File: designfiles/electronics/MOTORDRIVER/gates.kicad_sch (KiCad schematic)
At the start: 38 parts, among them IC14 LM5109BSDX_NOPB, IC15 LM5109BSDX_NOPB, IC16 LM5109BSDX_NOPB, IC17 LM5109BSDX_NOPB, IC18 INA2181A2IDGSR, Q22 30V 71A, Q23 30V 71A, Q24 30V 71A, Q25 30V 71A, Q26 30V 71A, Q27 30V 71A, Q28 30V 71A

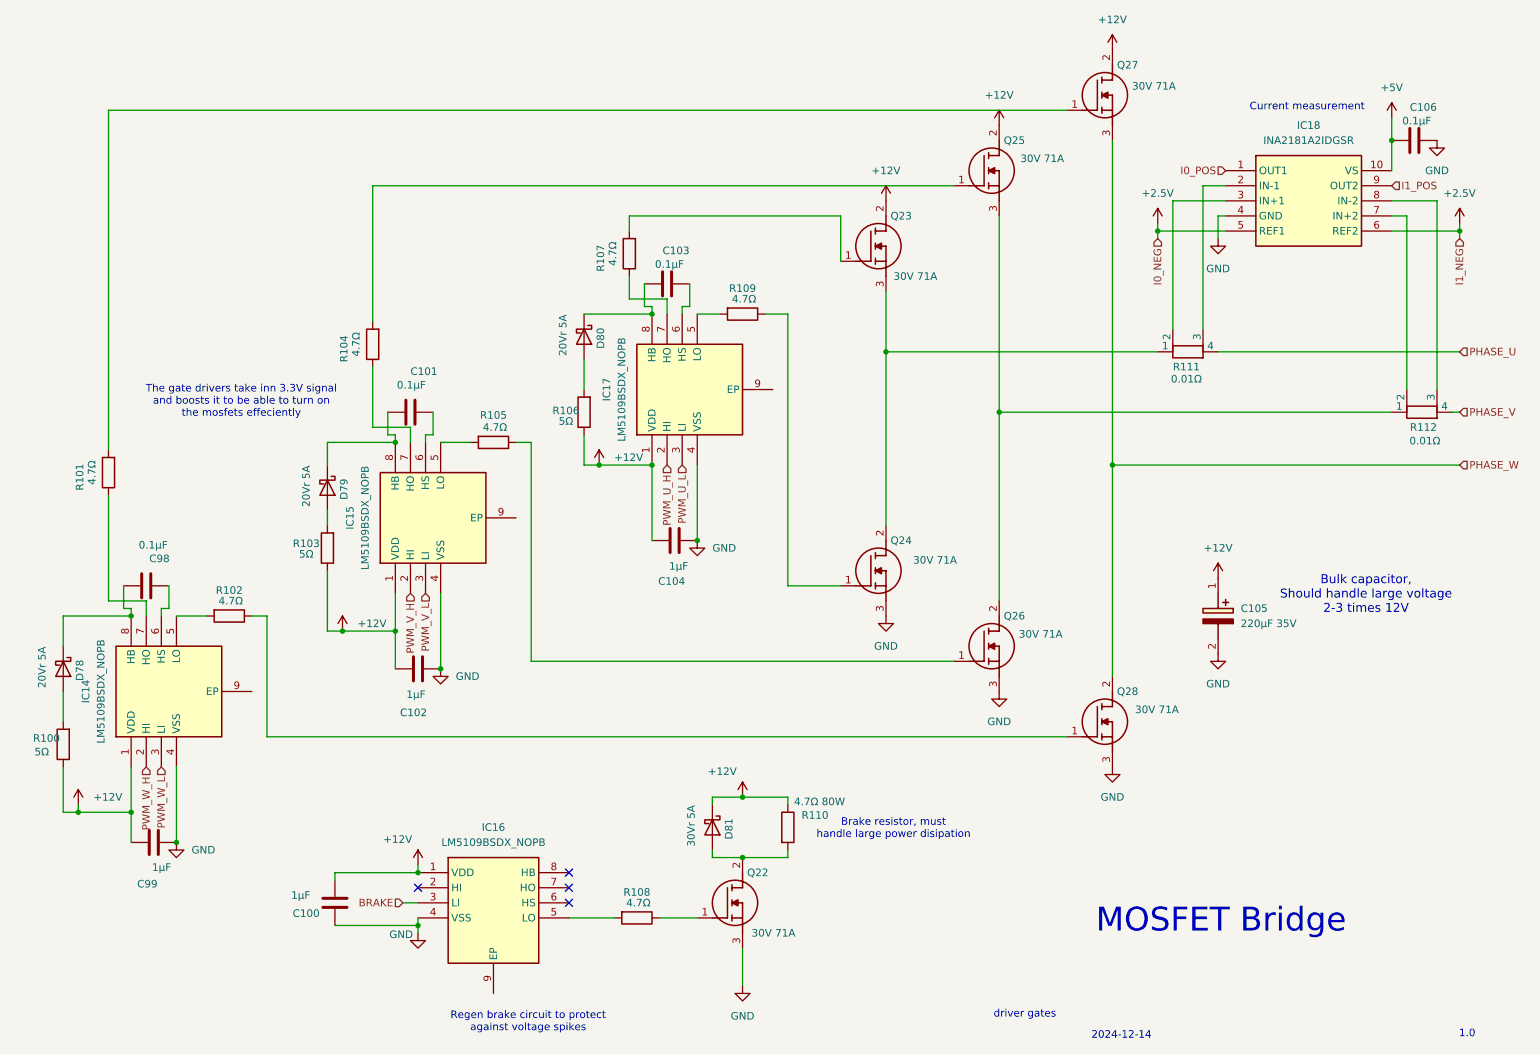
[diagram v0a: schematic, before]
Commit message: made clearer foldernames and cleaned up
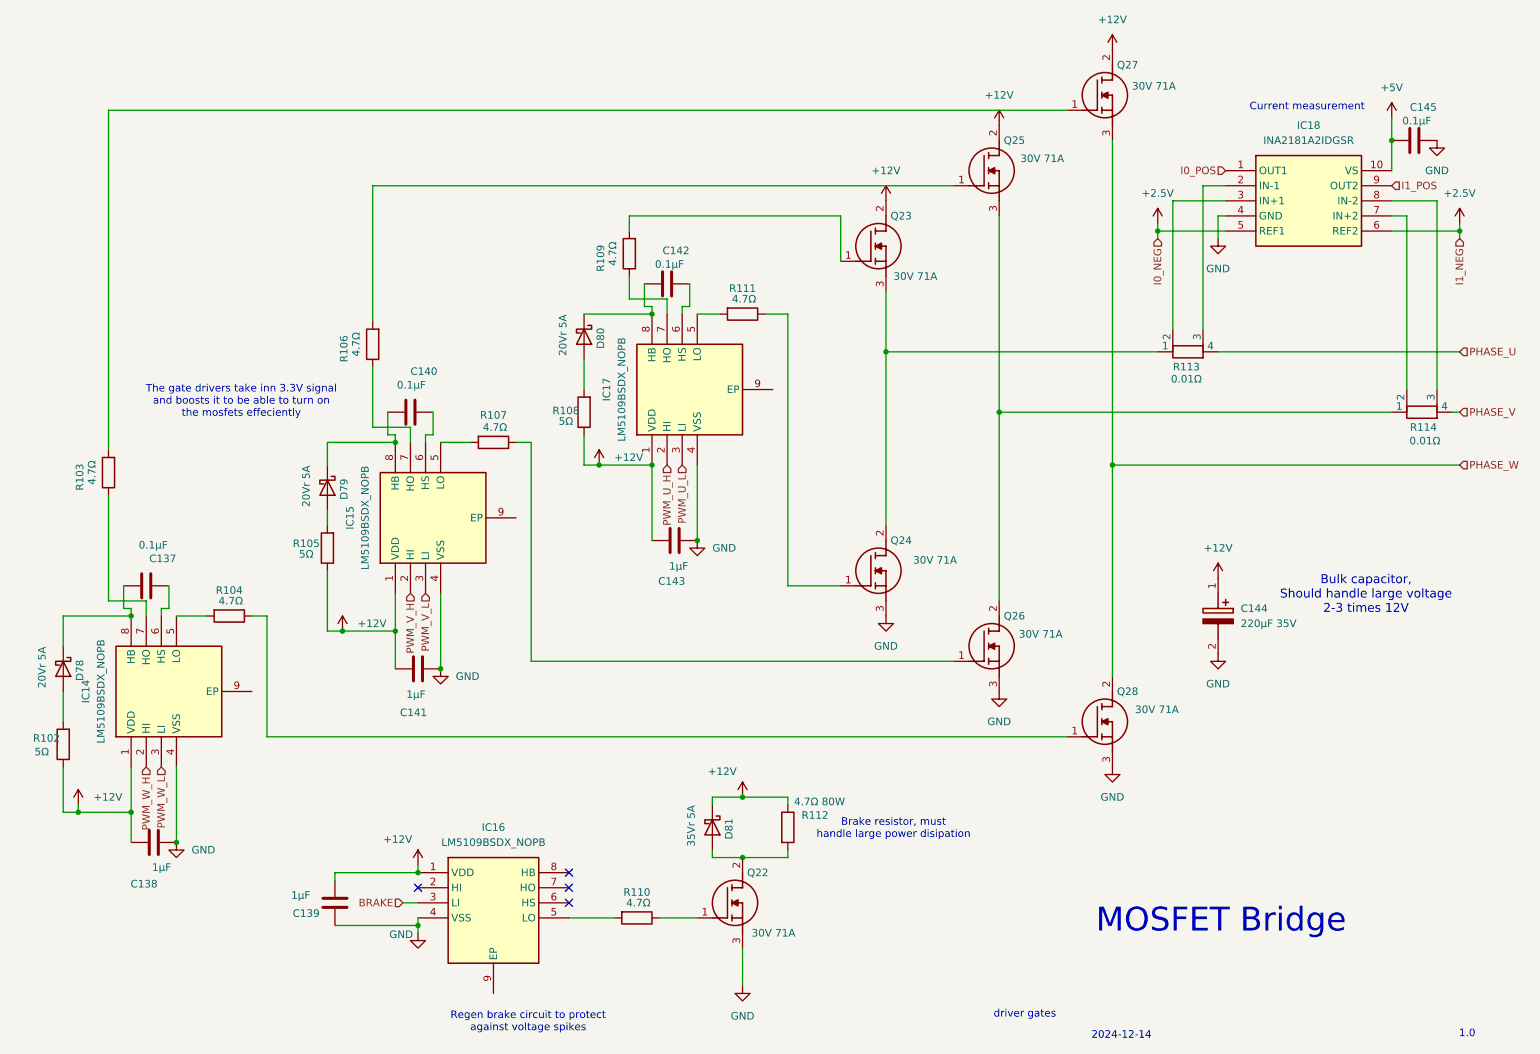
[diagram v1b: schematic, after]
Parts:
- D81: value 30Vr 5A -> 35Vr 5A
- renumbered C98 to C137, C99 to C138, C100 to C139, C101 to C140, C102 to C141, C103 to C142, C104 to C143, C105 to C144, C106 to C145, R100 to R102, R101 to R103, R102 to R104, R103 to R105, R104 to R106, R105 to R107, R106 to R108, R107 to R109, R108 to R110, R109 to R111, R110 to R112, R111 to R113, R112 to R114

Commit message: removed backup files and found components for special resistors and diodes
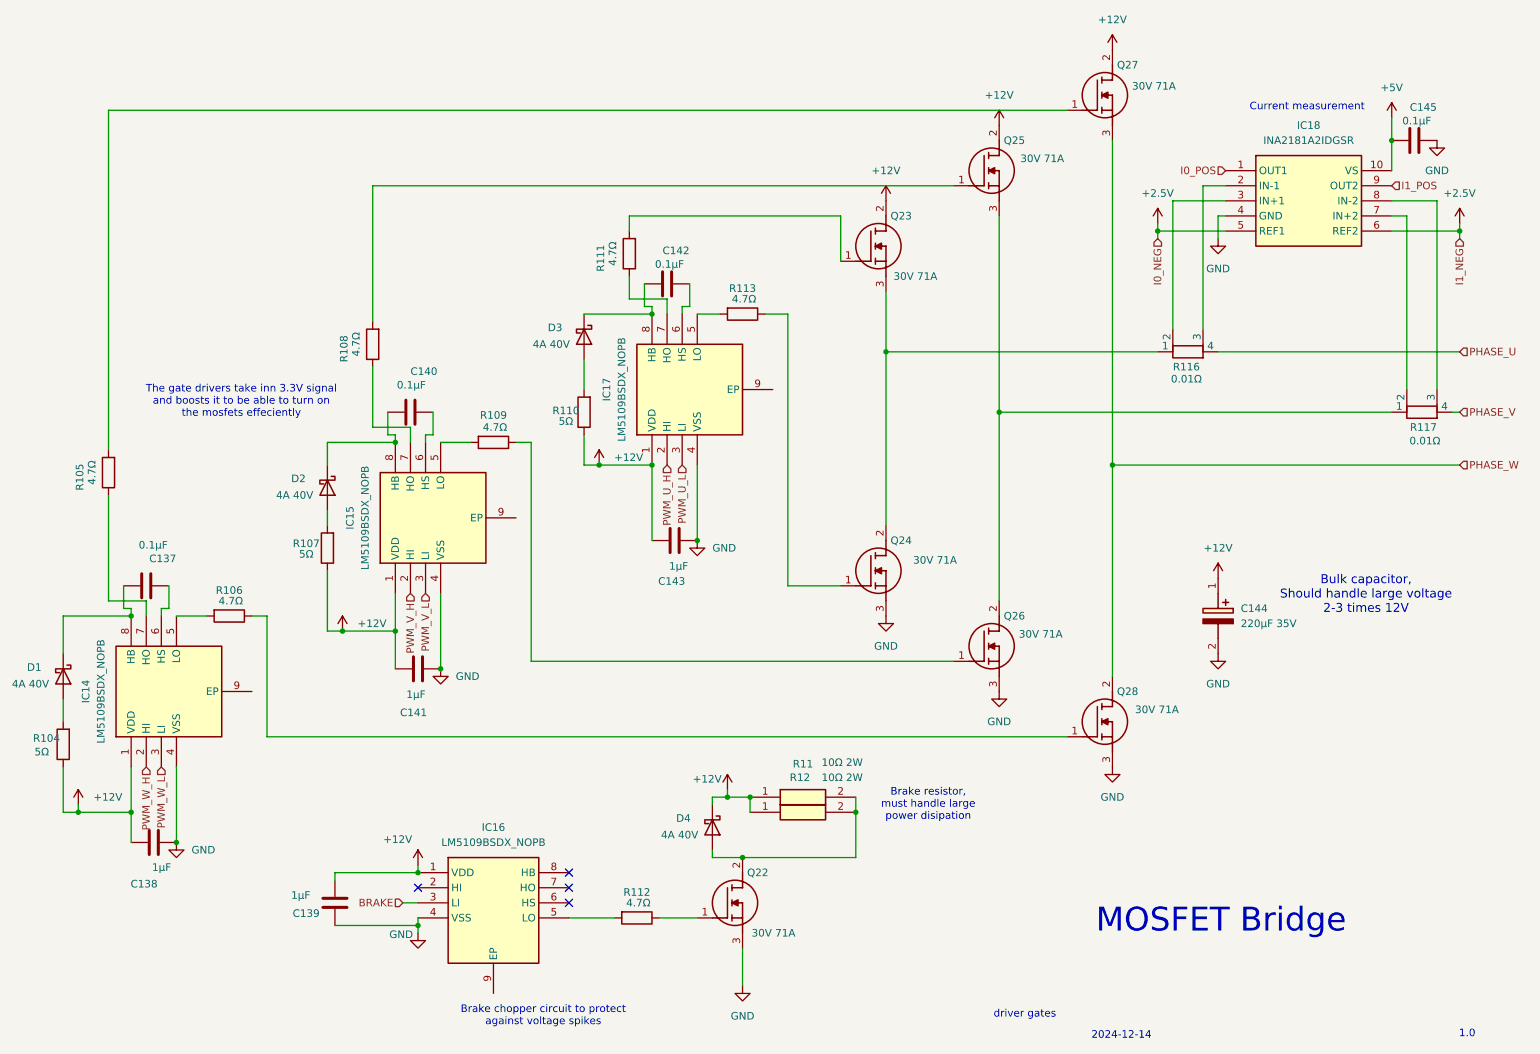
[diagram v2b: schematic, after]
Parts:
- removed D78, D79, D80: 20Vr 5A, Diode_SMD:D_0603_1608Metric, symbol Device:D_Schottky
- removed D81: 35Vr 5A, Diode_SMD:D_0603_1608Metric, symbol Device:D_Schottky
- removed R112: 4.7Ω 80W, Resistor_SMD:R_0603_1608Metric, symbol Device:R
- added D1, D2, D3, D4: 4A 40V, kuben-footprints:DIOM7959X262N, symbol Device:D_Schottky
- added R11, R12: 10Ω 2W, kuben-footprints:RESC3263X80N, symbol RCL122510R0FKEG:RCL122510R0FKEG
- renumbered R102 to R104, R103 to R105, R104 to R106, R105 to R107, R106 to R108, R107 to R109, R108 to R110, R109 to R111, R110 to R112, R111 to R113, R113 to R116, R114 to R117
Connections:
- net +12V: now also D4.1 (K), R11.1, R12.1
- net at R104.2: now also D1.2 (A)
- net at C140.2, IC15.8 (HB): now also D2.1 (K)
- net at C142.2, IC17.8 (HB): now also D3.1 (K)
- net at Q22.2 (D): now also D4.2 (A), R11.2, R12.2
- net at R110.2: now also D3.2 (A)
- net at C137.2, IC14.8 (HB): now also D1.1 (K)
- net at R107.2: now also D2.2 (A)
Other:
- note added: "Brake chopper circuit to protect against voltage spikes"
- note removed: "Regen brake circuit to protect against voltage spikes"

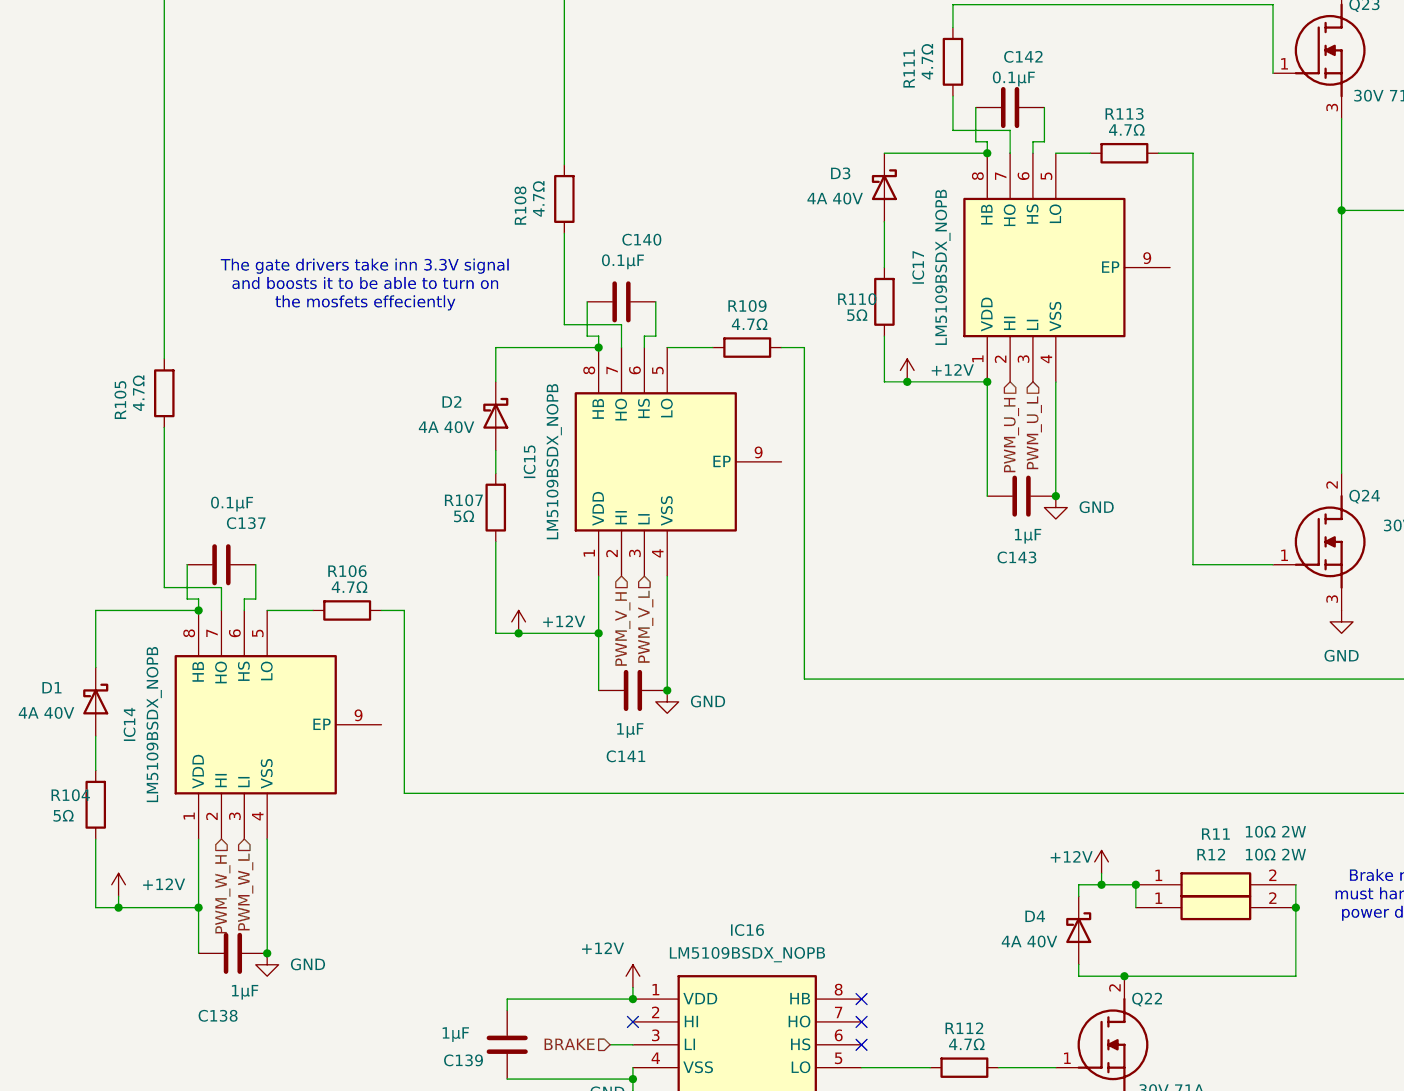
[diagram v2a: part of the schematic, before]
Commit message: added diodes
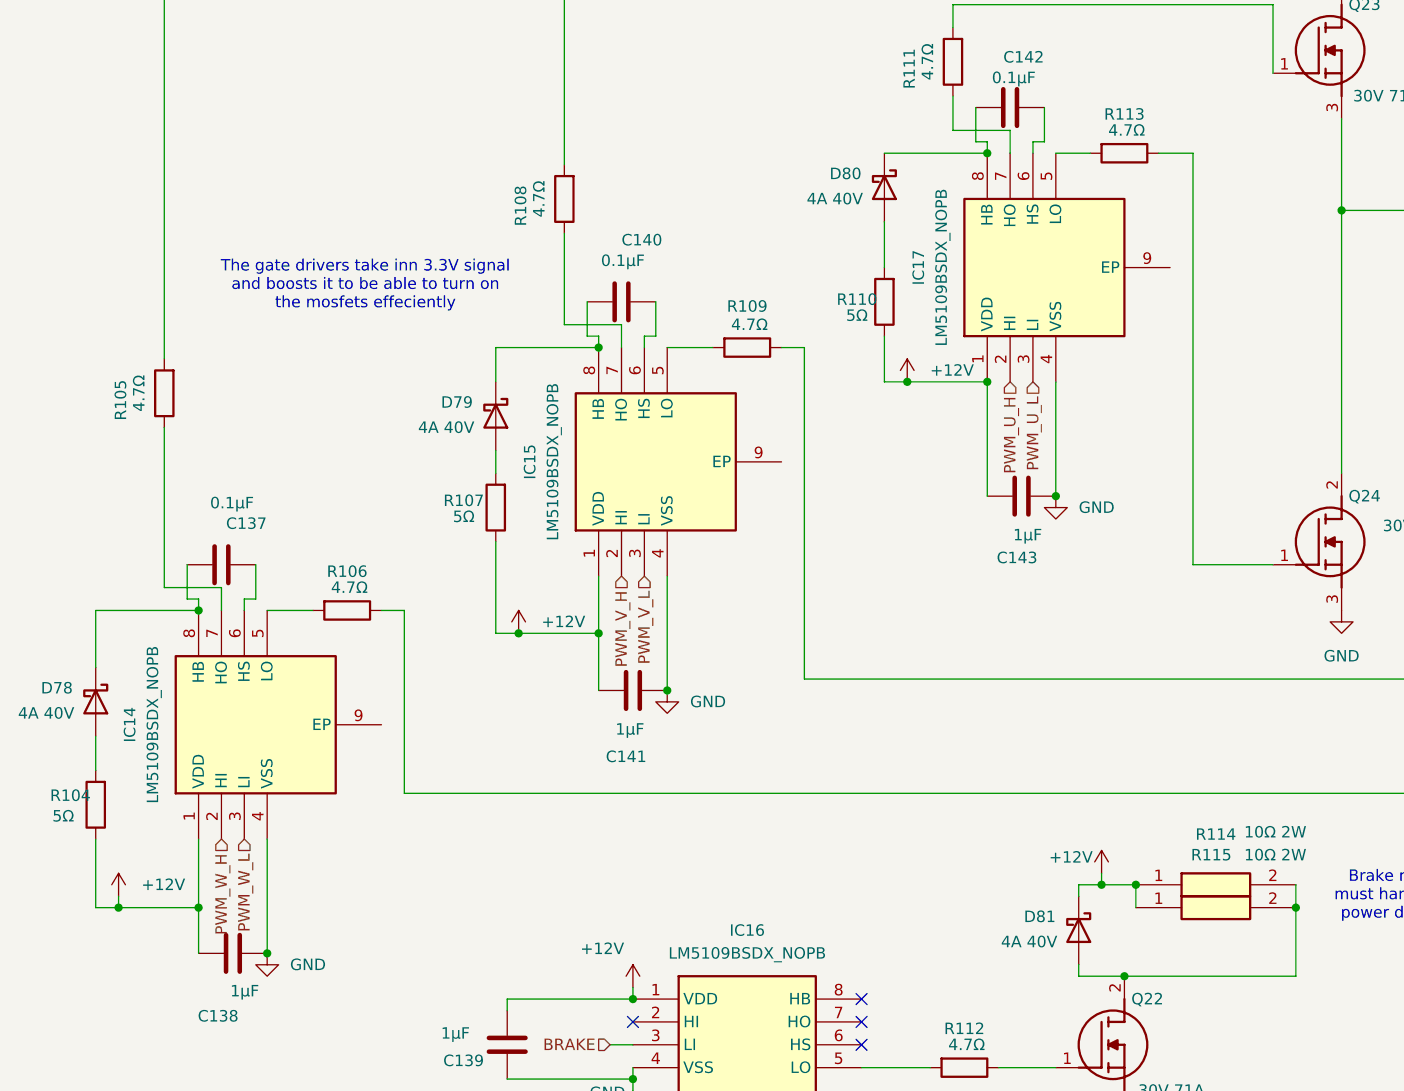
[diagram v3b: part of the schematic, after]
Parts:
- renumbered D1 to D78, D2 to D79, D3 to D80, D4 to D81, R11 to R114, R12 to R115
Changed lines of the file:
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@@
 		(on_board yes)
 		(dnp no)
-		(property "Reference" "D1"
+		(property "Reference" "D78"
 			(at 28.194 131.826 90)
 			(effects
@@
 		(on_board yes)
 		(dnp no)
-		(property "Reference" "D2"
+		(property "Reference" "D79"
 			(at 72.644 100.076 90)
 			(effects
@@
 		(on_board yes)
 		(dnp no)
-		(property "Reference" "R11"
+		(property "Reference" "R114"
 			(at 158.75 148.082 0)
 			(effects
@@
 		(on_board yes)
 		(dnp no)
-		(property "Reference" "R12"
+		(property "Reference" "R115"
 			(at 158.242 150.368 0)
 			(effects
@@
 		(on_board yes)
 		(dnp no)
-		(property "Reference" "D4"
+		(property "Reference" "D81"
 			(at 137.414 157.226 90)
 			(effects
@@
 		(on_board yes)
 		(dnp no)
-		(property "Reference" "D3"
+		(property "Reference" "D80"
 			(at 115.824 74.676 90)
 			(effects

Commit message: small tweaks
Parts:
- renumbered C137 to C144, C138 to C145, C139 to C146, C140 to C147, C141 to C148, C142 to C149, C143 to C150, C144 to C151, C145 to C152
